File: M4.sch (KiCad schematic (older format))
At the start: 181 parts, among them J1 PJ-301B, J10 PJ-301B, J11 PJ-301B, J12 PJ-301B, J13 PJ-301B, J2 PJ-301B, J3 PJ-301B, J4 PJ-301B, J5 PJ-301B, J6 PJ-301B, J7 PJ-301B, J8 PJ-301B, J9 PJ-301B, P1 CONN_01X01, P2 CONN_01X01, P3 CONN_01X01, P4 CONN_01X01, P5 CONN_01X06, P6 CONN_02X05, P7 CONN_01X01, SW1 B3F-1050, SW2 B3F-1050, SW3 B3F-1050, SW4 B3F-1050, SW5 B3F-1050, SW6 B3F-1050, SW7 B3F-1050, U1 LM1117, U10 STM32F410RBTx, U2 MCP1703, U3 MAX5134, U4 74ACT541, U5 OPA4171, U6 OPA171, U7 OPA171, U8 CD4051, U9 OPA4171, X1 MIDI IN, Y1 8MHz

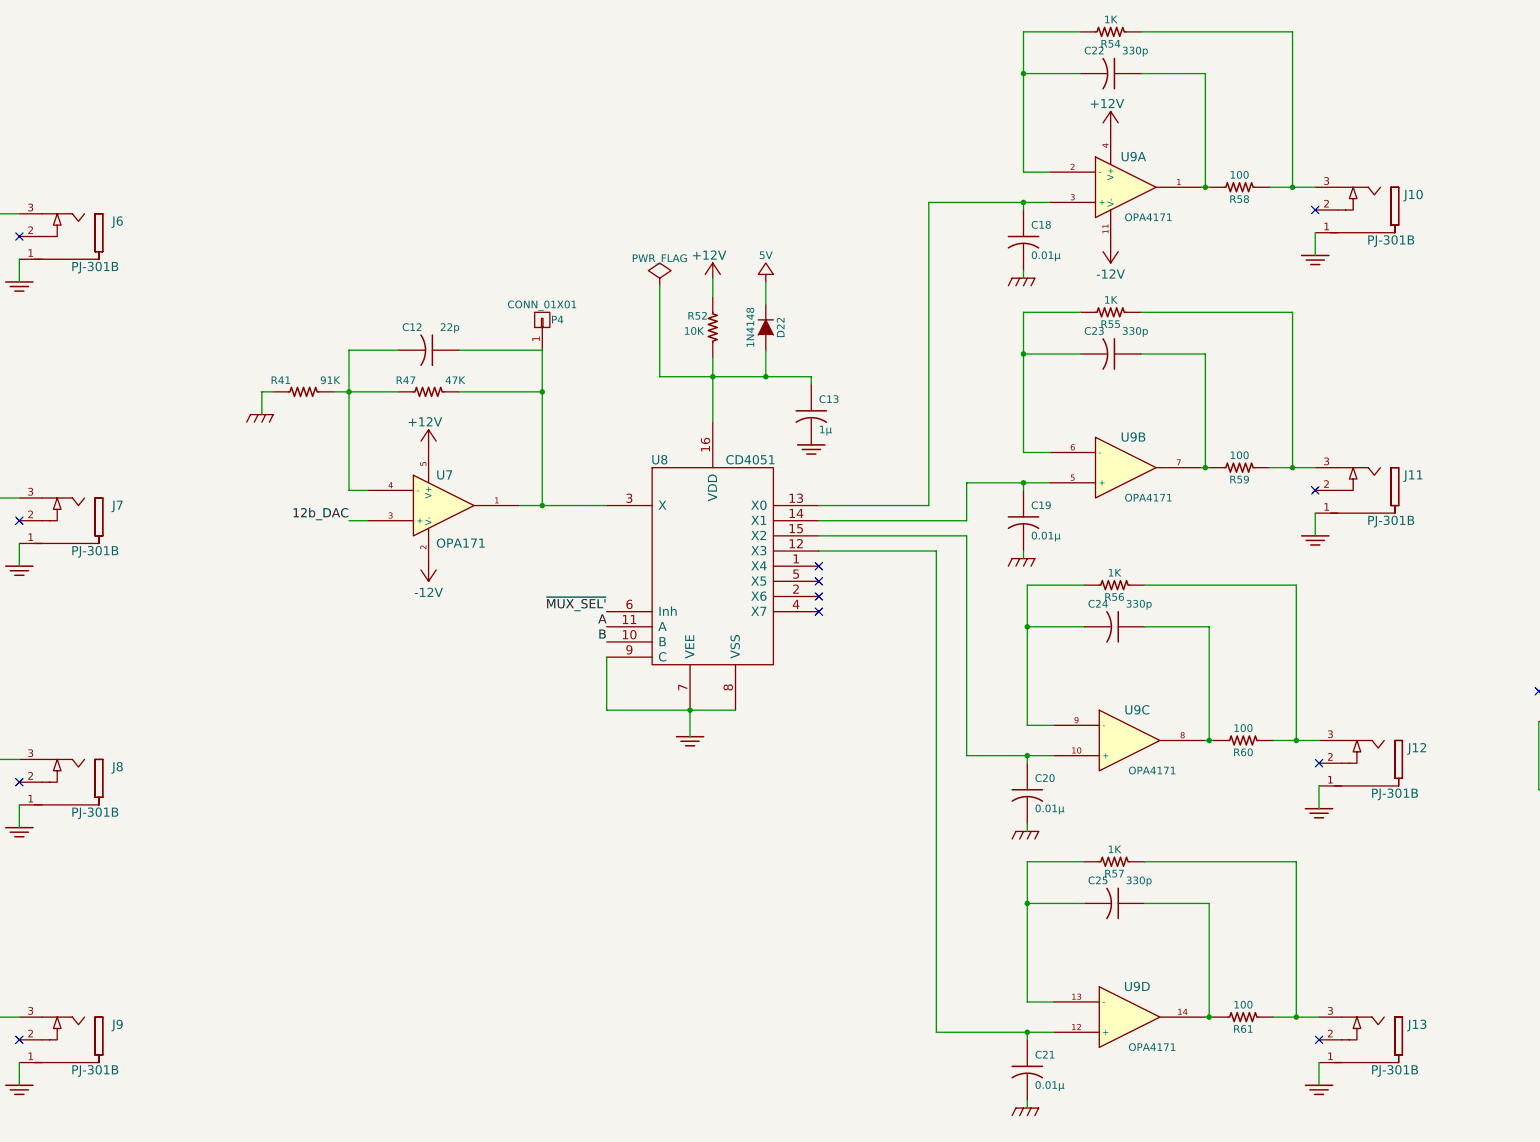
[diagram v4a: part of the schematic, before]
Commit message: basically routed. need to delete excess decoupling caps and decide about whether external sw pull up resistors are necessary - probably not and need to be deleted
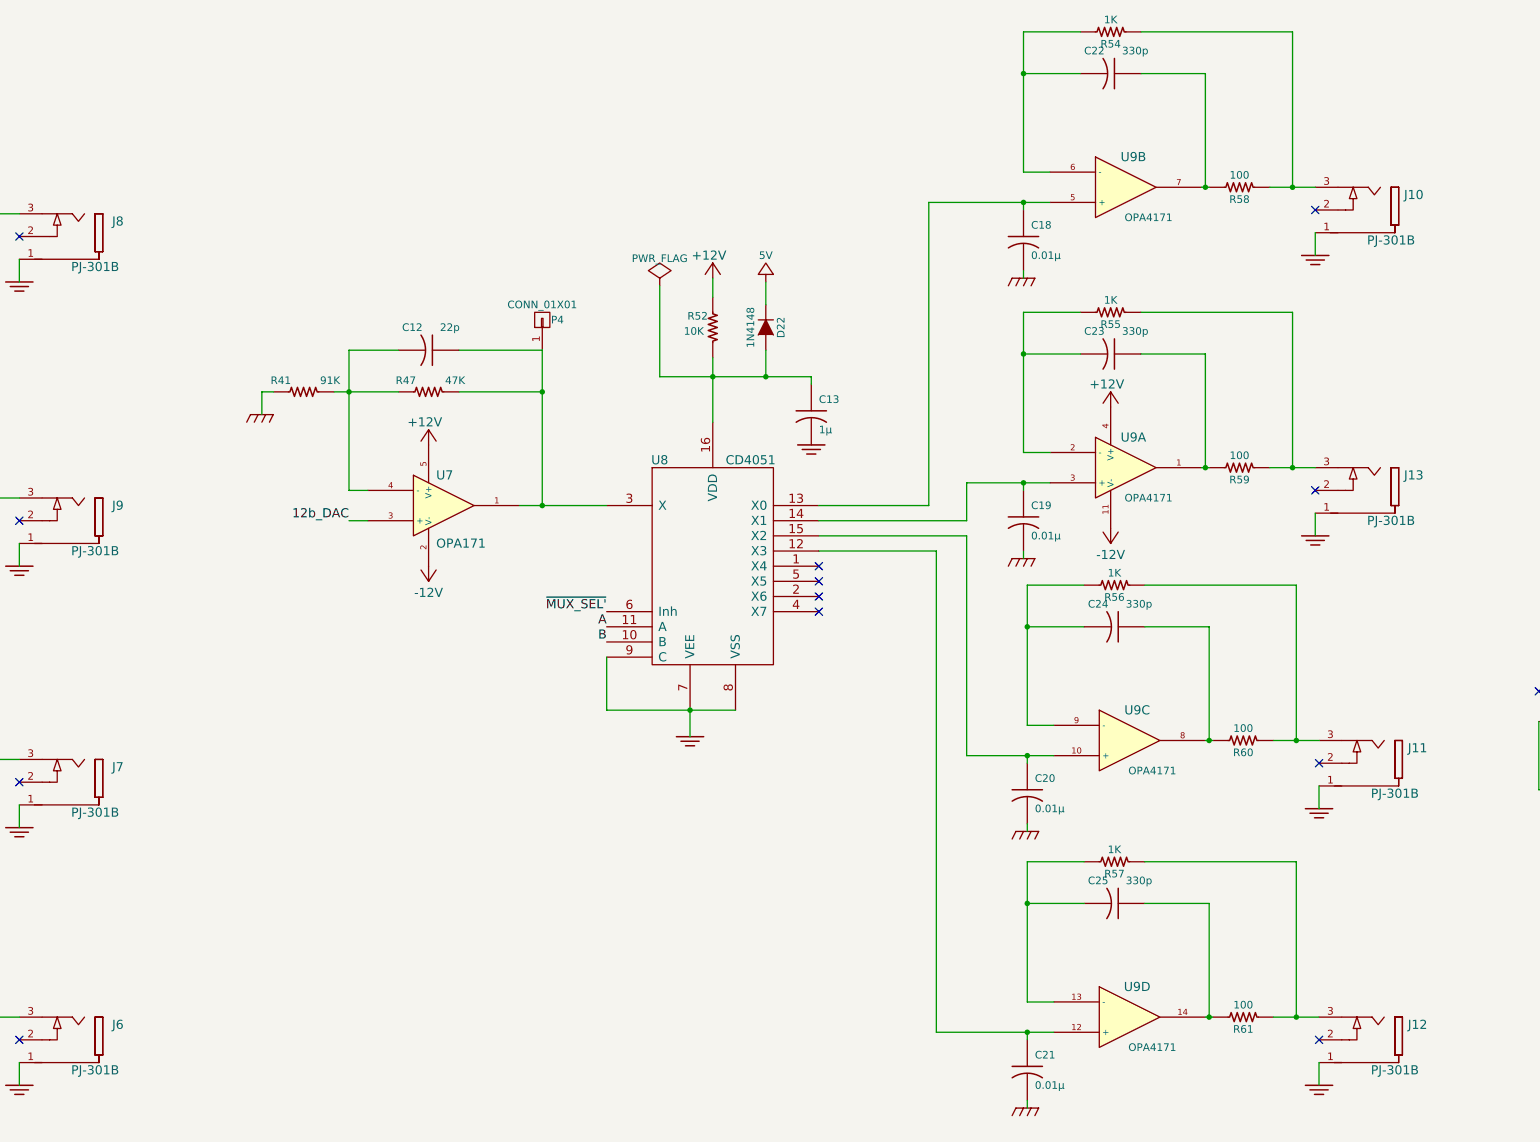
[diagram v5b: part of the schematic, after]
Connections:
- net at C18.1, U8.13 (X0): now also U9.5 (+); no longer U9.3 (+)
- net at C19.1, U8.14 (X1): now also U9.3 (+); no longer U9.5 (+)
- net at R17.1, R18.1: now also J8.3; no longer J6.3
- net at R15.1, R20.1: now also J7.3; no longer J8.3
- net at R16.1, R21.1: now also J6.3; no longer J9.3
- net at R14.1, R19.1: now also J9.3; no longer J7.3
- net at C22.1, R58.2: now also U9.7; no longer U9.1
- net at C22.2, R54.2: now also U9.6 (-); no longer U9.2 (-)
- net at C23.2, R55.2: now also U9.2 (-); no longer U9.6 (-)
- net at C23.1, R59.2: now also U9.1; no longer U9.7
- net at R55.1, R59.1: now also J13.3; no longer J11.3
- net at R56.1, R60.1: now also J11.3; no longer J12.3
- net at R57.1, R61.1: now also J12.3; no longer J13.3
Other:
- moved on the sheet: J11, J12, J13, J6, J7, J8, J9, U9A, U9B
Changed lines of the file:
@@
 L JACK_MONO_SW J6
 U 1 1 58C77209
-P 6675 2175
-F 0 "J6" H 6275 2075 60  0000 C CNN
-F 1 "PJ-301B" H 6425 2375 60  0000 C CNN
-F 2 "MyModules:PJ-301B-JACK-SLOTS" H 6575 2175 60  0001 C CNN
-F 3 "" H 6575 2175 60  0000 C CNN
-	1    6675 2175
+P 6675 7475
+F 0 "J6" H 6275 7375 60  0000 C CNN
+F 1 "PJ-301B" H 6425 7675 60  0000 C CNN
+F 2 "MyModules:PJ-301B-JACK-SLOTS" H 6575 7475 60  0001 C CNN
+F 3 "" H 6575 7475 60  0000 C CNN
+	1    6675 7475
 	-1   0    0    1
 $EndComp
@@
 L JACK_MONO_SW J8
 U 1 1 58C7BF31
-P 6675 5775
-F 0 "J8" H 6275 5675 60  0000 C CNN
-F 1 "PJ-301B" H 6425 5975 60  0000 C CNN
-F 2 "MyModules:PJ-301B-JACK-SLOTS" H 6575 5775 60  0001 C CNN
-F 3 "" H 6575 5775 60  0000 C CNN
-	1    6675 5775
+P 6675 2175
+F 0 "J8" H 6275 2075 60  0000 C CNN
+F 1 "PJ-301B" H 6425 2375 60  0000 C CNN
+F 2 "MyModules:PJ-301B-JACK-SLOTS" H 6575 2175 60  0001 C CNN
+F 3 "" H 6575 2175 60  0000 C CNN
+	1    6675 2175
 	-1   0    0    1
 $EndComp
@@
 L JACK_MONO_SW J9
 U 1 1 58C7BF57
-P 6675 7475
-F 0 "J9" H 6275 7375 60  0000 C CNN
-F 1 "PJ-301B" H 6425 7675 60  0000 C CNN
-F 2 "MyModules:PJ-301B-JACK-SLOTS" H 6575 7475 60  0001 C CNN
-F 3 "" H 6575 7475 60  0000 C CNN
-	1    6675 7475
+P 6675 4050
+F 0 "J9" H 6275 3950 60  0000 C CNN
+F 1 "PJ-301B" H 6425 4250 60  0000 C CNN
+F 2 "MyModules:PJ-301B-JACK-SLOTS" H 6575 4050 60  0001 C CNN
+F 3 "" H 6575 4050 60  0000 C CNN
+	1    6675 4050
 	-1   0    0    1
 $EndComp
@@
 L JACK_MONO_SW J7
 U 1 1 58C8671C
-P 6675 4050
-F 0 "J7" H 6275 3950 60  0000 C CNN
-F 1 "PJ-301B" H 6425 4250 60  0000 C CNN
-F 2 "MyModules:PJ-301B-JACK-SLOTS" H 6575 4050 60  0001 C CNN
-F 3 "" H 6575 4050 60  0000 C CNN
-	1    6675 4050
+P 6675 5775
+F 0 "J7" H 6275 5675 60  0000 C CNN
+F 1 "PJ-301B" H 6425 5975 60  0000 C CNN
+F 2 "MyModules:PJ-301B-JACK-SLOTS" H 6575 5775 60  0001 C CNN
+F 3 "" H 6575 5775 60  0000 C CNN
+	1    6675 5775
 	-1   0    0    1
 $EndComp
@@
 L +12V #PWR085
 U 1 1 58D1FC82
-P 13625 1450
-F 0 "#PWR085" H 13625 1550 30  0001 C CNN
-F 1 "+12V" H 13600 1600 60  0000 C CNN
-F 2 "~" H 13625 1450 60  0000 C CNN
-F 3 "~" H 13625 1450 60  0000 C CNN
-	1    13625 1450
+P 13625 3300
+F 0 "#PWR085" H 13625 3400 30  0001 C CNN
+F 1 "+12V" H 13600 3450 60  0000 C CNN
+F 2 "~" H 13625 3300 60  0000 C CNN
+F 3 "~" H 13625 3300 60  0000 C CNN
+	1    13625 3300
 	1    0    0    -1
 $EndComp
@@
 L -12V #PWR086
 U 1 1 58D1FC88
-P 13625 2250
-F 0 "#PWR086" H 13625 2350 30  0001 C CNN
-F 1 "-12V" H 13625 2425 60  0000 C CNN
-F 2 "~" H 13625 2250 60  0000 C CNN
-F 3 "~" H 13625 2250 60  0000 C CNN
-	1    13625 2250
+P 13625 4100
+F 0 "#PWR086" H 13625 4200 30  0001 C CNN
+F 1 "-12V" H 13625 4275 60  0000 C CNN
+F 2 "~" H 13625 4100 60  0000 C CNN
+F 3 "~" H 13625 4100 60  0000 C CNN
+	1    13625 4100
 	-1   0    0    1
 $EndComp
@@
 L TL074- U9
 U 1 1 58D1FC8E
-P 13725 1850
-F 0 "U9" H 13775 2050 60  0000 C CNN
-F 1 "OPA4171" H 13875 1650 50  0000 C CNN
-F 2 "Housings_SSOP:TSSOP-14_4.4x5mm_Pitch0.65mm" H 13725 1850 60  0001 C CNN
-F 3 "" H 13725 1850 60  0000 C CNN
-	1    13725 1850
+P 13725 3700
+F 0 "U9" H 13775 3900 60  0000 C CNN
+F 1 "OPA4171" H 13875 3500 50  0000 C CNN
+F 2 "Housings_SSOP:TSSOP-14_4.4x5mm_Pitch0.65mm" H 13725 3700 60  0001 C CNN
+F 3 "" H 13725 3700 60  0000 C CNN
+	1    13725 3700
 	1    0    0    -1
 $EndComp
@@
 L TL074- U9
 U 2 1 58D3B4CD
-P 13725 3700
-F 0 "U9" H 13775 3900 60  0000 C CNN
-F 1 "OPA4171" H 13875 3500 50  0000 C CNN
-F 2 "Housings_SSOP:TSSOP-14_4.4x5mm_Pitch0.65mm" H 13725 3700 60  0001 C CNN
-F 3 "" H 13725 3700 60  0000 C CNN
-	2    13725 3700
+P 13725 1850
+F 0 "U9" H 13775 2050 60  0000 C CNN
+F 1 "OPA4171" H 13875 1650 50  0000 C CNN
+F 2 "Housings_SSOP:TSSOP-14_4.4x5mm_Pitch0.65mm" H 13725 1850 60  0001 C CNN
+F 3 "" H 13725 1850 60  0000 C CNN
+	2    13725 1850
 	1    0    0    -1
 $EndComp
@@
 L JACK_MONO_SW J11
 U 1 1 58D3B4FE
-P 15225 3850
-F 0 "J11" H 14825 3750 60  0000 C CNN
-F 1 "PJ-301B" H 14975 4050 60  0000 C CNN
-F 2 "MyModules:PJ-301B-JACK-SLOTS" H 15125 3850 60  0001 C CNN
-F 3 "" H 15125 3850 60  0000 C CNN
-	1    15225 3850
+P 15250 5650
+F 0 "J11" H 14850 5550 60  0000 C CNN
+F 1 "PJ-301B" H 15000 5850 60  0000 C CNN
+F 2 "MyModules:PJ-301B-JACK-SLOTS" H 15150 5650 60  0001 C CNN
+F 3 "" H 15150 5650 60  0000 C CNN
+	1    15250 5650
 	-1   0    0    1
 $EndComp
@@
 L JACK_MONO_SW J12
 U 1 1 58D3CE13
-P 15250 5650
-F 0 "J12" H 14850 5550 60  0000 C CNN
-F 1 "PJ-301B" H 15000 5850 60  0000 C CNN
-F 2 "MyModules:PJ-301B-JACK-SLOTS" H 15150 5650 60  0001 C CNN
-F 3 "" H 15150 5650 60  0000 C CNN
-	1    15250 5650
+P 15250 7475
+F 0 "J12" H 14850 7375 60  0000 C CNN
+F 1 "PJ-301B" H 15000 7675 60  0000 C CNN
+F 2 "MyModules:PJ-301B-JACK-SLOTS" H 15150 7475 60  0001 C CNN
+F 3 "" H 15150 7475 60  0000 C CNN
+	1    15250 7475
 	-1   0    0    1
 $EndComp
@@
 L JACK_MONO_SW J13
 U 1 1 58D3E0DB
-P 15250 7475
-F 0 "J13" H 14850 7375 60  0000 C CNN
-F 1 "PJ-301B" H 15000 7675 60  0000 C CNN
-F 2 "MyModules:PJ-301B-JACK-SLOTS" H 15150 7475 60  0001 C CNN
-F 3 "" H 15150 7475 60  0000 C CNN
-	1    15250 7475
+P 15225 3850
+F 0 "J13" H 14825 3750 60  0000 C CNN
+F 1 "PJ-301B" H 14975 4050 60  0000 C CNN
+F 2 "MyModules:PJ-301B-JACK-SLOTS" H 15125 3850 60  0001 C CNN
+F 3 "" H 15125 3850 60  0000 C CNN
+	1    15225 3850
 	-1   0    0    1
 $EndComp

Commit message: changed LED models to TLUGX240
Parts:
- removed Y1: 8MHz, synth:403-XTAL-4-SMD, symbol Crystal
- added Y1: 4-SMD-XTAL, symbol 4-SMD-XTAL
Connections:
- net at C14.2, U10.5 (PH0/RCC_OSC_IN): now also Y1.1
- net at C15.2, U10.6 (PH1/RCC_OSC_OUT): now also Y1.3
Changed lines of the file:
@@
-$EndComp
-$Comp
-L Crystal Y1
-U 1 1 58C7B0FE
-P 12150 12375
-F 0 "Y1" V 12025 12500 50  0000 C CNN
-F 1 "8MHz" V 12150 12700 50  0000 C CNN
-F 2 "synth:403-XTAL-4-SMD" H 12150 12375 60  0001 C CNN
-F 3 "" H 12150 12375 60  0000 C CNN
-	1    12150 12375
-	0    1    1    0
 $EndComp
 $Comp
@@
 Text Label 4625 2125 2    60   ~ 0
 DAC_CH3
+$Comp
+L 4-SMD-XTAL Y1
+U 1 1 58CE2AD5
+P 12150 12375
+F 0 "Y1" V 12150 12525 50  0000 C CNN
+F 1 "4-SMD-XTAL" V 12325 12625 50  0000 C CNN
+F 2 "" H 12150 12375 60  0000 C CNN
+F 3 "" H 12150 12375 60  0000 C CNN
+	1    12150 12375
+	0    1    1    0
+$EndComp
 $EndSCHEMATC
